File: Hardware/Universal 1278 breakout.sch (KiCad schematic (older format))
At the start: 7 parts, among them J1 Conn_Coaxial, J2 Conn_01x10, J3 Conn_01x10, U1 XL1278-SMT, U2 DRF1278F

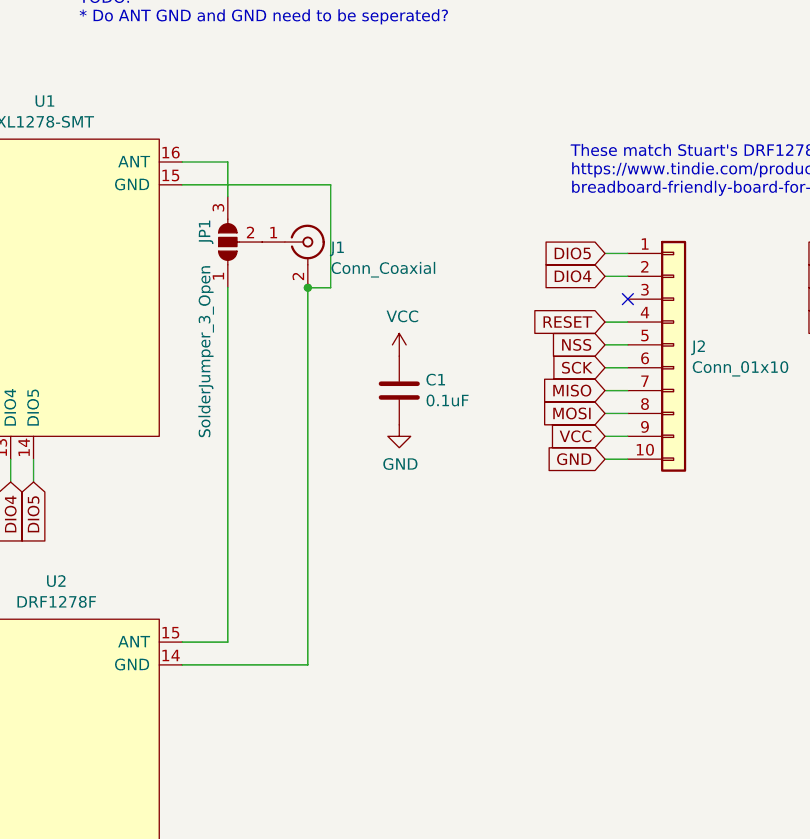
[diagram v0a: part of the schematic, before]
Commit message: Fix (most) DRC errors.
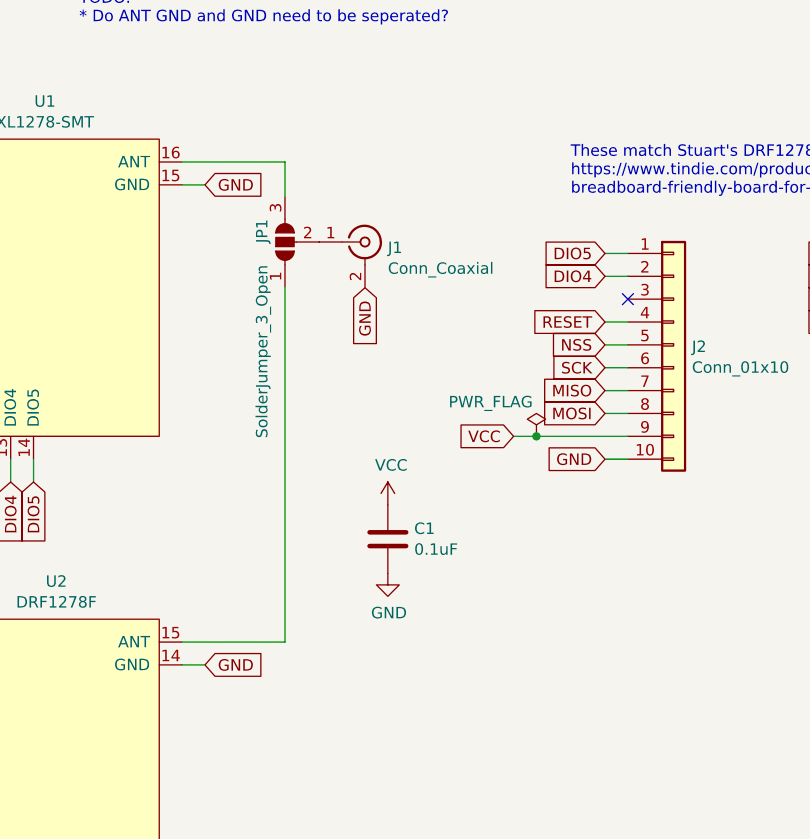
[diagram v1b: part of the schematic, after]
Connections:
- net GND: now also J1.2 (Ext), U1.15 (GND), U2.14 (GND)
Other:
- moved on the sheet: C1, J1, JP1
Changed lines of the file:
@@
 L Connector:Conn_Coaxial J1
 U 1 1 60306FAD
-P 4900 2150
-F 0 "J1" H 5000 2125 50  0000 L CNN
-F 1 "Conn_Coaxial" H 5000 2034 50  0000 L CNN
-F 2 "Connector_Coaxial:SMA_Molex_73251-2120_EdgeMount_Horizontal" H 4900 2150 50  0001 C CNN
-F 3 " ~" H 4900 2150 50  0001 C CNN
-	1    4900 2150
+P 5150 2150
+F 0 "J1" H 5250 2125 50  0000 L CNN
+F 1 "Conn_Coaxial" H 5250 2034 50  0000 L CNN
+F 2 "Connector_Coaxial:SMA_Molex_73251-2120_EdgeMount_Horizontal" H 5150 2150 50  0001 C CNN
+F 3 " ~" H 5150 2150 50  0001 C CNN
+	1    5150 2150
 	1    0    0    -1
 $EndComp
@@
 Text GLabel 3050 4600 0    50   Input ~ 0
 VCC
-Wire Wire Line
-	3050 4600 3150 4600
-Wire Wire Line
-	4350 4000 4900 4000
-Wire Wire Line
-	4900 4000 4900 2350
-Text GLabel 6200 3000 0    50   Input ~ 0
+Text GLabel 5800 3000 0    50   Input ~ 0
 VCC
 Text GLabel 6200 3100 0    50   Input ~ 0
@@
 	6200 3100 6300 3100
 Wire Wire Line
-	6200 3000 6300 3000
+	5800 3000 5900 3000
 Text GLabel 3050 4700 0    50   Input ~ 0
 GND
@@
 MOSI
 $Comp
+L Jumper:SolderJumper_3_Open JP1
+U 1 1 60334856
+P 4800 2150
+F 0 "JP1" H 4900 2250 50  0000 R CNN
+F 1 "SolderJumper_3_Open" H 4700 2250 50  0000 R CNN
+F 2 "Jumper:SolderJumper-3_P1.3mm_Open_RoundedPad1.0x1.5mm" H 4800 2150 50  0001 C CNN
+F 3 "~" H 4800 2150 50  0001 C CNN
+	1    4800 2150
+	0    -1   -1   0
+$EndComp
+$Comp
 L Device:C C1
 U 1 1 6035BFEB
-P 5300 2800
-F 0 "C1" H 5415 2846 50  0000 L CNN
-F 1 "0.1uF" H 5415 2755 50  0000 L CNN
-F 2 "Capacitors_SMD:C_0603_HandSoldering" H 5338 2650 50  0001 C CNN
-F 3 "~" H 5300 2800 50  0001 C CNN
-	1    5300 2800
+P 5250 3450
+F 0 "C1" H 5365 3496 50  0000 L CNN
+F 1 "0.1uF" H 5365 3405 50  0000 L CNN
+F 2 "Capacitors_SMD:C_0603_HandSoldering" H 5288 3300 50  0001 C CNN
+F 3 "~" H 5250 3450 50  0001 C CNN
+	1    5250 3450
+	1    0    0    -1
+$EndComp
+$Comp
+L power:VCC #PWR0102
+U 1 1 6035CD5F
+P 5250 3300
+F 0 "#PWR0102" H 5250 3150 50  0001 C CNN
+F 1 "VCC" H 5265 3473 50  0000 C CNN
+F 2 "" H 5250 3300 50  0001 C CNN
+F 3 "" H 5250 3300 50  0001 C CNN
+	1    5250 3300
 	1    0    0    -1
 $EndComp
@@
 L power:GND #PWR0101
 U 1 1 6035C5C3
-P 5300 2950
-F 0 "#PWR0101" H 5300 2700 50  0001 C CNN
-F 1 "GND" H 5305 2777 50  0000 C CNN
-F 2 "" H 5300 2950 50  0001 C CNN
-F 3 "" H 5300 2950 50  0001 C CNN
-	1    5300 2950
-	1    0    0    -1
-$EndComp
-$Comp
-L power:VCC #PWR0102
-U 1 1 6035CD5F
-P 5300 2650
-F 0 "#PWR0102" H 5300 2500 50  0001 C CNN
-F 1 "VCC" H 5315 2823 50  0000 C CNN
-F 2 "" H 5300 2650 50  0001 C CNN
-F 3 "" H 5300 2650 50  0001 C CNN
-	1    5300 2650
-	1    0    0    -1
-$EndComp
-$Comp
-L Jumper:SolderJumper_3_Open JP1
-U 1 1 60334856
-P 4550 2150
-F 0 "JP1" H 4650 2250 50  0000 R CNN
-F 1 "SolderJumper_3_Open" H 4450 2250 50  0000 R CNN
-F 2 "Jumper:SolderJumper-3_P1.3mm_Open_RoundedPad1.0x1.5mm" H 4550 2150 50  0001 C CNN
-F 3 "~" H 4550 2150 50  0001 C CNN
-	1    4550 2150
-	0    -1   -1   0
-$EndComp
+P 5250 3600
+F 0 "#PWR0101" H 5250 3350 50  0001 C CNN
+F 1 "GND" H 5255 3427 50  0000 C CNN
+F 2 "" H 5250 3600 50  0001 C CNN
+F 3 "" H 5250 3600 50  0001 C CNN
+	1    5250 3600
+	1    0    0    -1
+$EndComp
+Text GLabel 4450 4000 2    50   Input ~ 0
+GND
+Text GLabel 4450 1900 2    50   Input ~ 0
+GND
+Wire Wire Line
+	4350 1900 4450 1900
+Wire Wire Line
+	4350 1800 4800 1800
+Wire Wire Line
+	4800 1800 4800 1950
 $Comp
 L My_library:DRF1278F U2
@@
 $EndComp
 Wire Wire Line
-	4350 1800 4550 1800
-Wire Wire Line
-	4550 1800 4550 1950
-Wire Wire Line
-	4550 2350 4550 3900
-Wire Wire Line
-	4550 3900 4350 3900
-Wire Wire Line
-	4350 1900 5000 1900
-Wire Wire Line
-	5000 1900 5000 2350
-Wire Wire Line
-	5000 2350 4900 2350
-Connection ~ 4900 2350
+	4350 4000 4450 4000
+Wire Wire Line
+	4350 3900 4800 3900
+Wire Wire Line
+	4800 3900 4800 2350
+Text GLabel 5150 2350 3    50   Input ~ 0
+GND
+Wire Wire Line
+	3050 4600 3150 4600
+$Comp
+L power:PWR_FLAG #FLG0101
+U 1 1 603B47C9
+P 5900 3000
+F 0 "#FLG0101" H 5900 3075 50  0001 C CNN
+F 1 "PWR_FLAG" H 5700 3150 50  0000 C CNN
+F 2 "" H 5900 3000 50  0001 C CNN
+F 3 "~" H 5900 3000 50  0001 C CNN
+	1    5900 3000
+	1    0    0    -1
+$EndComp
+Connection ~ 5900 3000
+Wire Wire Line
+	5900 3000 6300 3000
 $EndSCHEMATC

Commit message: Various updates.
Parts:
- J1: footprint Connector_Coaxial:SMA_Molex_73251-2120_EdgeMount_Horizontal -> My footprints:SMA_EdgeMount_Holes
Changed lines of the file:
@@
 U 1 1 60306FAD
 P 5150 2150
-F 0 "J1" H 5250 2125 50  0000 L CNN
-F 1 "Conn_Coaxial" H 5250 2034 50  0000 L CNN
-F 2 "Connector_Coaxial:SMA_Molex_73251-2120_EdgeMount_Horizontal" H 5150 2150 50  0001 C CNN
+F 0 "J1" H 5250 1950 50  0000 L CNN
+F 1 "Conn_Coaxial" H 5250 1850 50  0000 L CNN
+F 2 "My footprints:SMA_EdgeMount_Holes" H 5150 2150 50  0001 C CNN
 F 3 " ~" H 5150 2150 50  0001 C CNN
 	1    5150 2150
@@
 Wire Wire Line
 	4800 3900 4800 2350
-Text GLabel 5150 2350 3    50   Input ~ 0
+Text GLabel 5150 2450 3    50   Input ~ 0
 GND
 Wire Wire Line
@@
 Wire Wire Line
 	5900 3000 6300 3000
+Wire Wire Line
+	5150 2350 5150 2450
 $EndSCHEMATC

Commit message: Update.
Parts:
- U1: footprint My footprints:XL1278-SMT -> Misc RF:XL1278-SMT; symbol My_library:XL1278-SMT -> Misc_RF:XL1278-SMT
- U2: footprint My footprints:DRF1278F -> Misc RF:DRF1278F; symbol My_library:DRF1278F -> Misc_RF:DRF1278F
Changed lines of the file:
@@
 $EndDescr
 $Comp
-L My_library:XL1278-SMT U1
+L Misc_RF:XL1278-SMT U1
 U 1 1 603034E0
 P 3750 2400
 F 0 "U1" H 3750 3265 50  0000 C CNN
 F 1 "XL1278-SMT" H 3750 3174 50  0000 C CNN
-F 2 "My footprints:XL1278-SMT" H 3750 3350 50  0001 C CNN
+F 2 "Misc RF:XL1278-SMT" H 3750 3350 50  0001 C CNN
 F 3 "http://www.hr-wt.com/html_products/XL1278-SMT-59.html" H 3750 3200 50  0001 C CNN
 	1    3750 2400
@@
 	4800 1800 4800 1950
 $Comp
-L My_library:DRF1278F U2
+L Misc_RF:DRF1278F U2
 U 1 1 60303A0F
 P 3750 4500
 F 0 "U2" H 3800 5365 50  0000 C CNN
 F 1 "DRF1278F" H 3800 5274 50  0000 C CNN
-F 2 "My footprints:DRF1278F" H 3750 5300 50  0001 C CNN
+F 2 "Misc RF:DRF1278F" H 3750 5300 50  0001 C CNN
 F 3 "http://www.dorji.com/docs/data/DRF1278F.pdf" H 3750 5300 50  0001 C CNN
 	1    3750 4500

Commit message: Further updates
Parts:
- removed JP1: SolderJumper_3_Open, Jumper:SolderJumper-3_P1.3mm_Open_RoundedPad1.0x1.5mm, symbol Jumper:SolderJumper_3_Open
- J1: footprint My footprints:SMA_EdgeMount_Holes -> Misc RF:SMA_EdgeMount_Holes
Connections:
- net at U1.16 (ANT): now also J1.1 (In), U2.15 (ANT)
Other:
- note removed: "TODO:\n* Do ANT GND and GND need to be seperated?"
- moved on the sheet: J1
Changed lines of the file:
@@
 L Connector:Conn_Coaxial J1
 U 1 1 60306FAD
-P 5150 2150
-F 0 "J1" H 5250 1950 50  0000 L CNN
-F 1 "Conn_Coaxial" H 5250 1850 50  0000 L CNN
-F 2 "My footprints:SMA_EdgeMount_Holes" H 5150 2150 50  0001 C CNN
-F 3 " ~" H 5150 2150 50  0001 C CNN
-	1    5150 2150
+P 5000 1800
+F 0 "J1" H 5100 1600 50  0000 L CNN
+F 1 "Conn_Coaxial" H 5100 1500 50  0000 L CNN
+F 2 "Misc RF:SMA_EdgeMount_Holes" H 5000 1800 50  0001 C CNN
+F 3 " ~" H 5000 1800 50  0001 C CNN
+	1    5000 1800
 	1    0    0    -1
 $EndComp
@@
 Wire Wire Line
 	3050 2900 3150 2900
-Text Notes 3900 1200 0    50   ~ 0
-TODO:\n* Do ANT GND and GND need to be seperated?
 Text GLabel 7350 3100 0    50   Input ~ 0
 GND
@@
 Text GLabel 3050 2400 0    50   Input ~ 0
 MOSI
-$Comp
-L Jumper:SolderJumper_3_Open JP1
-U 1 1 60334856
-P 4800 2150
-F 0 "JP1" H 4900 2250 50  0000 R CNN
-F 1 "SolderJumper_3_Open" H 4700 2250 50  0000 R CNN
-F 2 "Jumper:SolderJumper-3_P1.3mm_Open_RoundedPad1.0x1.5mm" H 4800 2150 50  0001 C CNN
-F 3 "~" H 4800 2150 50  0001 C CNN
-	1    4800 2150
-	0    -1   -1   0
-$EndComp
 $Comp
 L Device:C C1
@@
 Wire Wire Line
 	4350 1800 4800 1800
-Wire Wire Line
-	4800 1800 4800 1950
 $Comp
 L Misc_RF:DRF1278F U2
@@
 	4350 3900 4800 3900
 Wire Wire Line
-	4800 3900 4800 2350
-Text GLabel 5150 2450 3    50   Input ~ 0
+	4800 3900 4800 1800
+Text GLabel 5000 2100 3    50   Input ~ 0
 GND
 Wire Wire Line
@@
 	5900 3000 6300 3000
 Wire Wire Line
-	5150 2350 5150 2450
+	5000 2000 5000 2100
+Connection ~ 4800 1800
 $EndSCHEMATC
